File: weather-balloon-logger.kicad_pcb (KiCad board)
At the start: 2 copper layers, 80 x 78.5 mm, 22 parts, among them J1 Conn_01x02, J2 Conn_01x11, J3 SMA, J4 SMA, J5 Conn_01x02, J6 VHF, J7 HF, Q1 AO3400A, SW1 SPDT, U1 PCF8574T

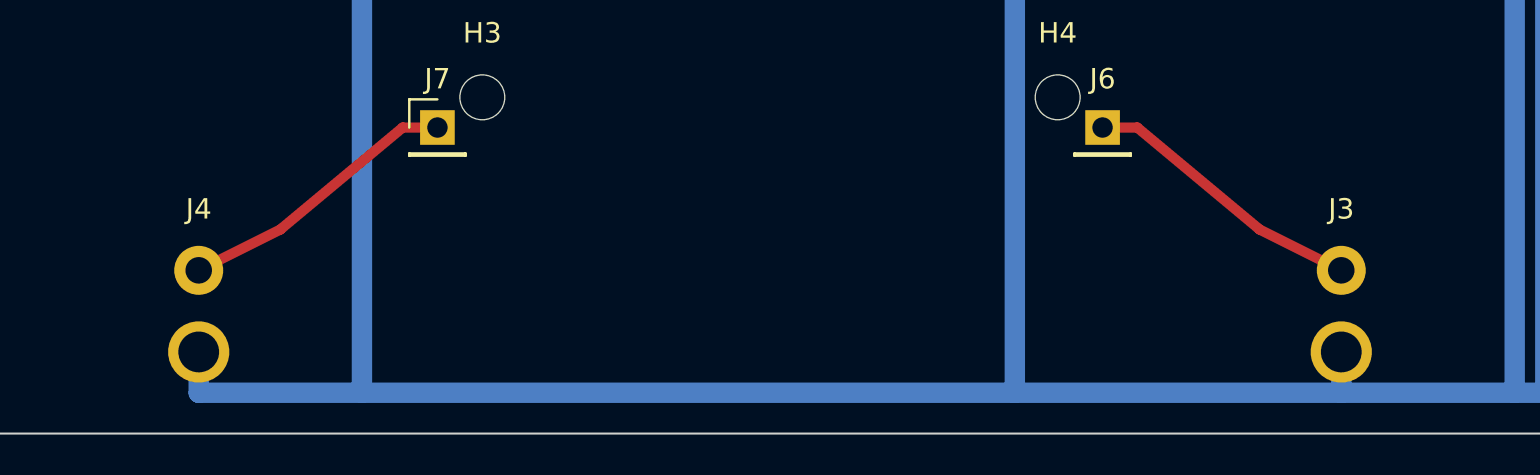
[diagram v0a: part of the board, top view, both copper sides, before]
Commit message: copperhead: SMA footprint/routing pass only. J3 and J4 now contain the exact KiCad footprints Connector_Coaxial:SMA_Amphenol_132134_Vertical, each with center pad 1 and four through-hole shield pads numbered 2. Their current positions are J3 (168,162) for RF_APRS and J4 (112,162) for RF_WSPR and must remain fixed; the footprints fit the outline and existing RF reservation.\n\nRepair only this real-footprint fallout:\n- Keep all footprints, orientations, and board edges fixed.\n- Preserve J6 RF_APRS to J3 center pad 1 and J7 RF_WSPR to J4 center pad 1.\n- Reroute only RF_APRS, RF_WSPR, and local GND so neither center conductor crosses or violates clearance to any shield pad.\n- Connect all four pad-2 shield tabs on each SMA solidly to GND using short symmetric local copper and/or nearby ground vias/trunk connections appropriate for a first-pass RF launch.\n- Remove dangling placeholder ground stubs.\n- Preserve the existing >=5 mm RF/mechanical reservation drawings and keep unrelated copper/components out.\n- Do not claim final 50-ohm qualification: document that trace geometry and return-via strategy still require released stackup calculation and VNA validation.\n- Preserve all six exact LightAPRS mechanical-interface exclusions; add no global DRC suppression.\n- Update docs/LAYOUT.md and docs/FOOTPRINT_AUDIT.md with the actual SMA pad/fanout result and remaining RF fabrication hold.\n- Run normal kicad-cli DRC and Copperhead checks. Commit this pass only with zero normal DRC violations and zero unconnected items.
Repaired only the exact J3/J4 SMA routing fallout. J6 RF_APRS remains connected to J3 pad 1 and J7 RF_WSPR remains connected to J4 pad 1 through 0.5 mm F.Cu centerline approaches that clear every shield pad. Each connector's four pad-2 shield tabs now use a short symmetric 1.0 mm B.Cu U-fanout tied to the existing bottom GND trunk, and both dangling placeholder stubs were removed. All footprints, orientations, board edges, RF reservation drawings, unrelate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
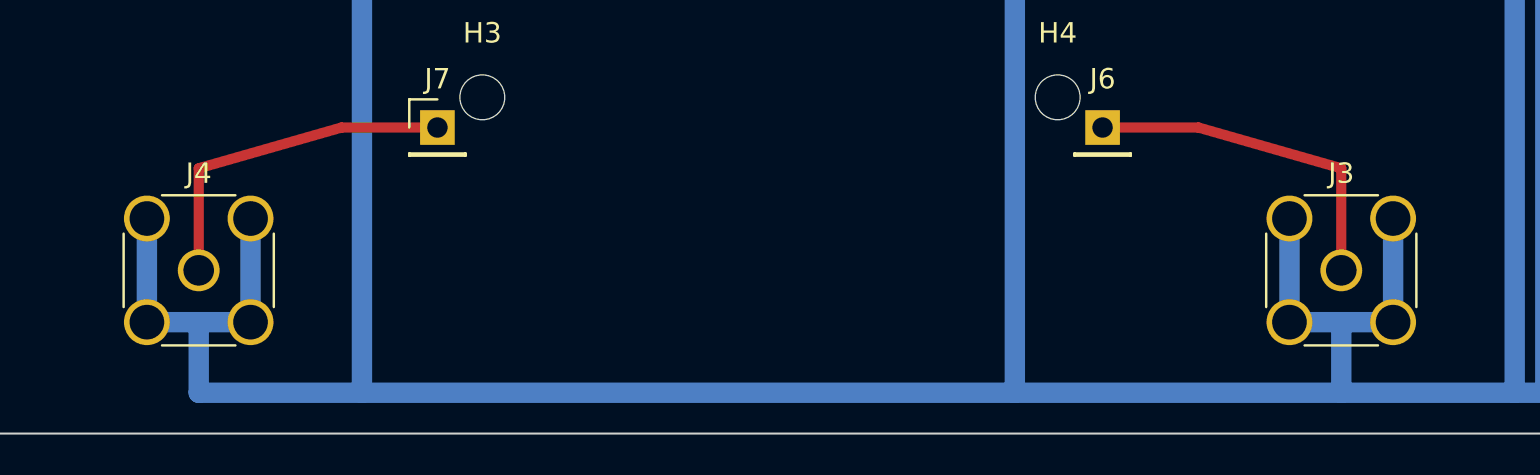
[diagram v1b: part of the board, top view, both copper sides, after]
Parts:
- J3, J4: footprint CopperheadDraft_SMA_Amphenol_132289 -> SMA_Amphenol_132134_Vertical
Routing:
- net GND: track 459.4 -> 492.8 mm
- net RF_WSPR: track 14.0 -> 17.0 mm
- net RF_APRS: track 14.0 -> 17.0 mm

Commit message: feat(pcb): route split logger supply
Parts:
- added A2: Pololu S7V8F5, Pololu_S7V8F5_Carrier, F.Cu at (106.0, 121.0)
- added R4: 1k, R_0603_1608Metric, F.Cu at (159.8, 113.3)
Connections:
- A1 pad 3: 3V3 -> LOGGER_5V
- A1 pad 5: UART_TX -> OPENLOG_RXI
- C1 pad 1: 3V3 -> LOGGER_5V
- C2 pad 1: 3V3 -> LOGGER_5V
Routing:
- net LOGGER_5V: track 0.00 -> 114.0 mm
- net 3V3: track 111.7 -> 71.3 mm
- net GND: track 492.8 -> 517.3 mm
- net PACK_SW: track 84.7 -> 92.8 mm
- net UART_TX: track 39.6 -> 42.6 mm
- net OPENLOG_RXI: track 0.00 -> 2.68 mm
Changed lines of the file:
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@@
 			(layers "F.Cu" "F.Mask" "F.Paste")
 			(roundrect_rratio 0.25)
-			(net "3V3")
+			(net "LOGGER_5V")
 		)
 		(pad "2" smd roundrect
@@
 			(layers "*.Cu" "*.Mask")
 			(remove_unused_layers no)
-			(net "3V3")
+			(net "LOGGER_5V")
 		)
 		(pad "4" thru_hole circle
@@
 			(layers "*.Cu" "*.Mask")
 			(remove_unused_layers no)
-			(net "UART_TX")
+			(net "OPENLOG_RXI")
 		)
 		(pad "6" thru_hole circle
@@
 			(layers "F.Cu" "F.Mask" "F.Paste")
 			(roundrect_rratio 0.25)
-			(net "3V3")
+			(net "LOGGER_5V")
 		)
 		(pad "2" smd roundrect
@@
 		(layer "Edge.Cuts")
 	)
+	(footprint "Pololu_S7V8F5_Carrier"
+		(layer "F.Cu")
+		(at 106 121 270)
+		(descr "Carrier land pattern for Pololu S7V8F5 item 2123, top-side and direct-soldered through the included 1x04 straight header; official 11.43 x 16.51 mm board and 1.02 mm holes")
+		(tags "Pololu S7V8F5 2123 buck boost regulator module carrier THT direct solder")
+		(property "Reference" "A2" (at 3.81 -16.55 0) (layer "F.SilkS") (effects (font (size 1 1) (thickness 0.15))))
+		(property "Value" "Pololu S7V8F5" (at 3.81 2.55 0) (layer "F.Fab") (effects (font (size 1 1) (thickness 0.15))))
+		(property "Datasheet" "https://www.pololu.com/product/2123" (at 0 0 0) (layer "F.Fab") (hide yes) (effects (font (size 1.27 1.27))))
+		(property "Description" "Pololu item 2123 S7V8F5 fixed 5 V step-up/step-down regulator module" (at 0 0 0) (layer "F.Fab") (hide yes) (effects (font (size 1.27 1.27))))
+		(attr through_hole board_only)
+		(duplicate_pad_numbers_are_jumpers no)
+		(fp_line (start -1.905 -15.24) (end 9.525 -15.24) (stroke (width 0.25) (type default)) (layer "F.SilkS"))
+		(fp_line (start -1.905 -15.24) (end -1.905 -1.35) (stroke (width 0.25) (type default)) (layer "F.SilkS"))
+		(fp_line (start 9.525 -15.24) (end 9.525 -1.35) (stroke (width 0.25) (type default)) (layer "F.SilkS"))
+		(fp_circle (center 7.62 -1.75) (end 8.02 -1.75) (stroke (width 0.2) (type default)) (fill no) (layer "F.SilkS"))
+		(fp_rect (start -2.405 -15.74) (end 10.025 1.77) (stroke (width 0.05) (type default)) (fill no) (layer "F.CrtYd"))
+		(fp_rect (start -1.905 -15.24) (end 9.525 1.27) (stroke (width 0.1) (type default)) (fill no) (layer "F.Fab"))
+		(fp_text user "TOP SIDE - DIRECT SOLDER" (at 3.81 -10.4 90) (layer "F.Fab") (effects (font (size 0.8 0.8) (thickness 0.12))))
+		(fp_text user "VOUT" (at 0 -2.4 90) (layer "F.Fab") (effects (font (size 0.65 0.65) (thickness 0.1))))
+		(fp_text user "GND" (at 2.54 -2.2 90) (layer "F.Fab") (effects (font (size 0.65 0.65) (thickness 0.1))))
+		(fp_text user "VIN" (at 5.08 -2.15 90) (layer "F.Fab") (effects (font (size 0.65 0.65) (thickness 0.1))))
+		(fp_text user "SHDN" (at 7.62 -2.45 90) (layer "F.Fab") (effects (font (size 0.65 0.65) (thickness 0.1))))
+		(pad "4" thru_hole circle (at 0 0) (size 1.8 1.8) (drill 1) (layers "*.Cu" "*.Mask") (remove_unused_layers no) (net "LOGGER_5V"))
+		(pad "3" thru_hole circle (at 2.54 0) (size 1.8 1.8) (drill 1) (layers "*.Cu" "*.Mask") (remove_unused_layers no) (net "GND"))
+		(pad "2" thru_hole circle (at 5.08 0) (size 1.8 1.8) (drill 1) (layers "*.Cu" "*.Mask") (remove_unused_layers no) (net "PACK_SW"))
+		(pad "1" thru_hole rect (at 7.62 0) (size 1.8 1.8) (drill 1) (layers "*.Cu" "*.Mask") (remove_unused_layers no) (net "PACK_SW"))
+		(embedded_fonts no)
+	)
+	(footprint "R_0603_1608Metric"
+		(layer "F.Cu")
+		(at 159.8 113.3 90)
+		(descr "Resistor SMD 0603 (1608 Metric), square (rectangular) end terminal, IPC-7351 nominal")
+		(tags "resistor")
+		(property "Reference" "R4" (at 0 -1.43 270) (layer "F.SilkS") (effects (font (size 1 1) (thickness 0.15))))
+		(property "Value" "1k" (at 0 1.43 270) (layer "F.Fab") (effects (font (size 1 1) (thickness 0.15))))
+		(property "Datasheet" "" (at 0 0 270) (layer "F.Fab") (hide yes) (effects (font (size 1.27 1.27))))
+		(property "Description" "" (at 0 0 270) (layer "F.Fab") (hide yes) (effects (font (size 1.27 1.27))))
+		(attr smd board_only)
+		(duplicate_pad_numbers_are_jumpers no)
+		(fp_line (start -0.237258 -0.5225) (end 0.237258 -0.5225) (stroke (width 0.12) (type solid)) (layer "F.SilkS"))
+		(fp_line (start -0.237258 0.5225) (end 0.237258 0.5225) (stroke (width 0.12) (type solid)) (layer "F.SilkS"))
+		(fp_rect (start -1.48 -0.73) (end 1.48 0.73) (stroke (width 0.05) (type solid)) (fill no) (layer "F.CrtYd"))
+		(fp_rect (start -0.8 -0.4125) (end 0.8 0.4125) (stroke (width 0.1) (type solid)) (fill no) (layer "F.Fab"))
+		(fp_text user "${REFERENCE}" (at 0 0 270) (layer "F.Fab") (effects (font (size 0.4 0.4) (thickness 0.06))))
+		(pad "1" smd roundrect (at -0.825 0 270) (size 0.8 0.95) (layers "F.Cu" "F.Mask" "F.Paste") (roundrect_rratio 0.25) (net "UART_TX"))
+		(pad "2" smd roundrect (at 0.825 0 270) (size 0.8 0.95) (layers "F.Cu" "F.Mask" "F.Paste") (roundrect_rratio 0.25) (net "OPENLOG_RXI"))
+		(embedded_fonts no)
+		(model "${KICAD10_3DMODEL_DIR}/Resistor_SMD.3dshapes/R_0603_1608Metric.step" (offset (xyz 0 0 0)) (scale (xyz 1 1 1)) (rotate (xyz 0 0 0)))
+	)
 	(gr_text "JAVAS Logger"
-		(at 114.5 118 0)
+		(at 110 96 0)
 		(layer "F.SilkS")
 		(effects
@@
 	(segment
 		(start 157 131.912)
-		(end 157 108)
-		(width 0.5)
-		(layer "F.Cu")
-		(net "3V3")
-	)
-	(segment
-		(start 157 108)
-		(end 156.5 108)
-		(width 0.5)
-		(layer "F.Cu")
-		(net "3V3")
-	)
-	(segment
-		(start 156.5 108)
-		(end 156.5 112)
+		(end 157 122.16)
 		(width 0.5)
 		(layer "F.Cu")
@@
 	)
 	(segment
-		(start 157 114)
-		(end 163.2 114)
-		(width 0.4)
-		(layer "F.Cu")
-		(net "3V3")
-	)
-	(segment
-		(start 165.92 110)
-		(end 167.2 114)
-		(width 0.4)
-		(layer "F.Cu")
-		(net "3V3")
-	)
-	(segment
 		(start 157 122.16)
 		(end 168.6 122.16)
@@
 		(net "3V3")
 	)
-	(segment
-		(start 156.5 112)
-		(end 165.92 112)
-		(width 0.5)
-		(layer "F.Cu")
-		(net "3V3")
-	)
-	(segment
-		(start 165.92 112)
-		(end 165.92 110)
-		(width 0.5)
-		(layer "F.Cu")
-		(net "3V3")
-	)
 	(via
 		(at 167 122.16)
@@
 	(segment
 		(start 150.5 106)
-		(end 160.84 106)
+		(end 155.8 106)
 		(width 0.3)
 		(layer "F.Cu")
@@
 	)
 	(segment
-		(start 160.84 106)
-		(end 160.84 110)
+		(start 155.8 106)
+		(end 155.8 114.125)
 		(width 0.3)
 		(layer "F.Cu")
 		(net "UART_TX")
 	)
+	(segment (start 155.8 114.125) (end 159.8 114.125) (width 0.3) (layer "F.Cu") (net "UART_TX"))
+	(segment (start 159.8 112.475) (end 160.84 110) (width 0.3) (layer "F.Cu") (net "OPENLOG_RXI"))
 	(segment
 		(start 154.9 129.364)
@@
 		(net "PACK_IN")
 	)
+	(segment (start 106 121) (end 101.2 121) (width 0.5) (layer "F.Cu") (net "LOGGER_5V"))
+	(segment (start 101.2 121) (end 101.2 98) (width 0.5) (layer "F.Cu") (net "LOGGER_5V"))
+	(segment (start 101.2 98) (end 106 98) (width 0.5) (layer "F.Cu") (net "LOGGER_5V"))
+	(segment (start 106 98) (end 165.92 98) (width 0.5) (layer "F.Cu") (net "LOGGER_5V"))
+	(segment (start 165.92 98) (end 165.92 110) (width 0.5) (layer "F.Cu") (net "LOGGER_5V"))
+	(segment (start 163.225 114) (end 163.225 112.5) (width 0.5) (layer "F.Cu") (net "LOGGER_5V"))
+	(segment (start 163.225 112.5) (end 167.225 112.5) (width 0.5) (layer "F.Cu") (net "LOGGER_5V"))
+	(segment (start 167.225 112.5) (end 167.225 114) (width 0.5) (layer "F.Cu") (net "LOGGER_5V"))
+	(segment (start 165.92 110) (end 165.92 112.5) (width 0.5) (layer "F.Cu") (net "LOGGER_5V"))
+	(segment (start 106 128.62) (end 106 126.08) (width 0.8) (layer "B.Cu") (net "PACK_SW"))
+	(segment (start 106 126.08) (end 111.636 126.08) (width 0.8) (layer "B.Cu") (net "PACK_SW"))
+	(segment (start 106 123.54) (end 108 123.54) (width 0.6) (layer "B.Cu") (net "GND"))
+	(segment (start 108 123.54) (end 108 106) (width 0.6) (layer "B.Cu") (net "GND"))
+	(segment (start 108 106) (end 103 106) (width 0.6) (layer "B.Cu") (net "GND"))
 	(embedded_fonts no)
 )
